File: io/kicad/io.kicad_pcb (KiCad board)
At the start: 2 copper layers, 90 x 88.4 mm, 52 parts, among them J1 Conn_01x04_Pin, J2 Conn_01x04_Pin, J3 pcie_98, U1 B0505MT-1WR4, U2 ESD5344D-TP, U3 ESD5344D-TP, U4 ADUM1201ARZ-RL7, U5 ADUM1201ARZ-RL7, U6 XC6206P332MR, U7 XC6206P332MR, U8 ESD5344D-TP

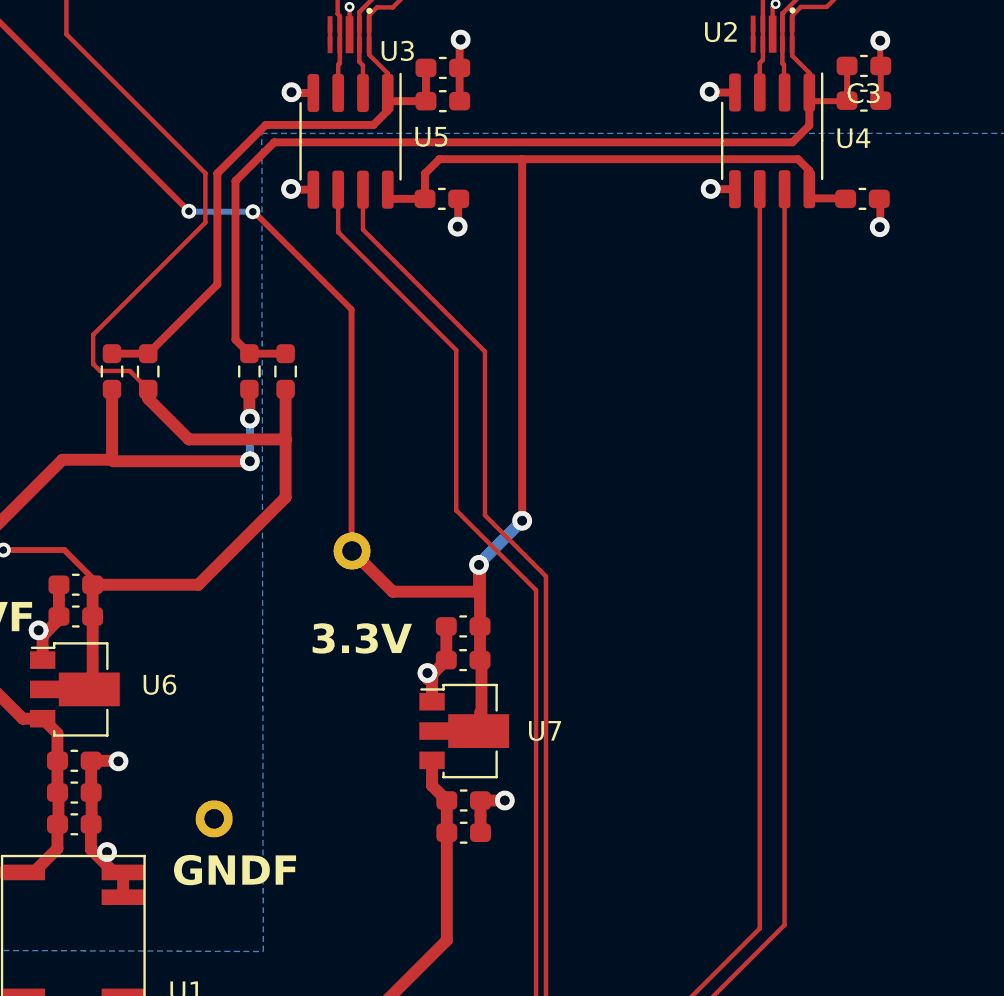
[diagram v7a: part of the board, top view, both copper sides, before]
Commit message: Tweaked the IO board layout.
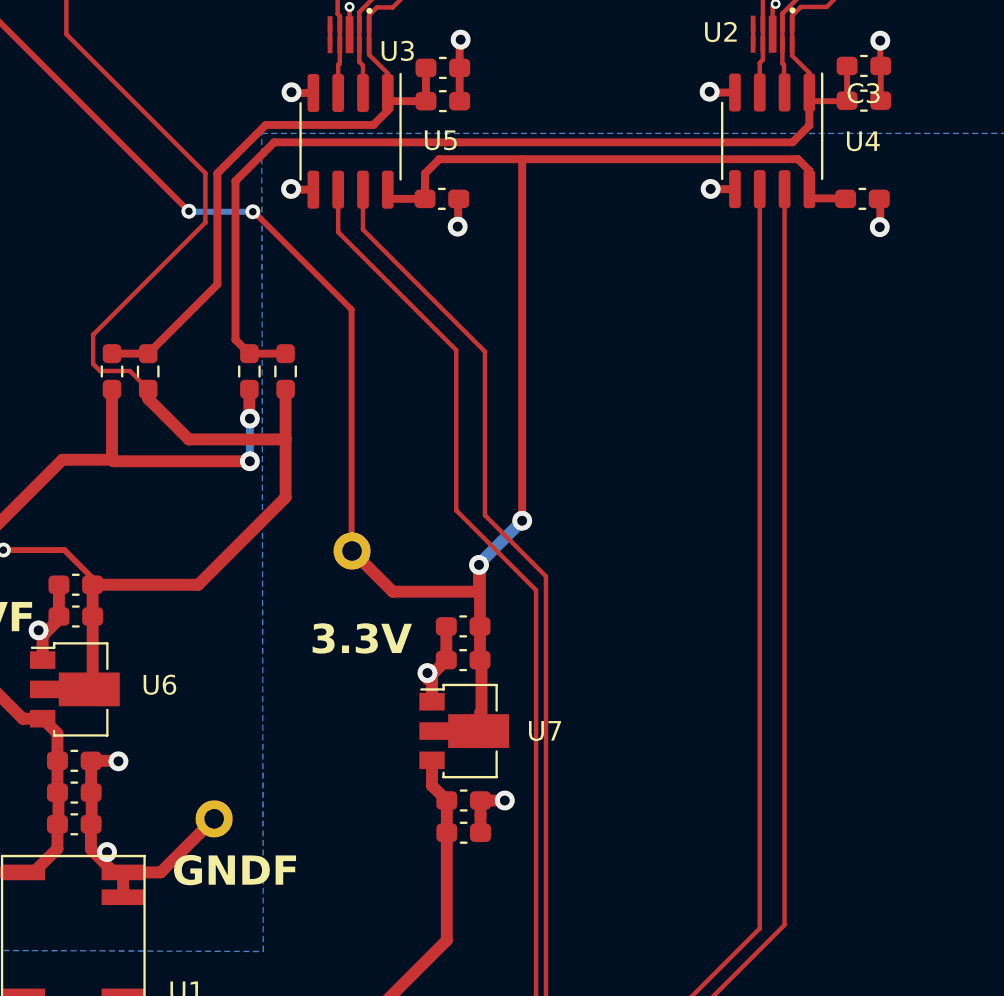
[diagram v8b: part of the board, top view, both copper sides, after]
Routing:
- net GND1: track 33.4 -> 39.2 mm
